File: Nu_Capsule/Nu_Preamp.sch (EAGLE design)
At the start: 20 parts, among them T1 2SC3324, T2 2SC3324

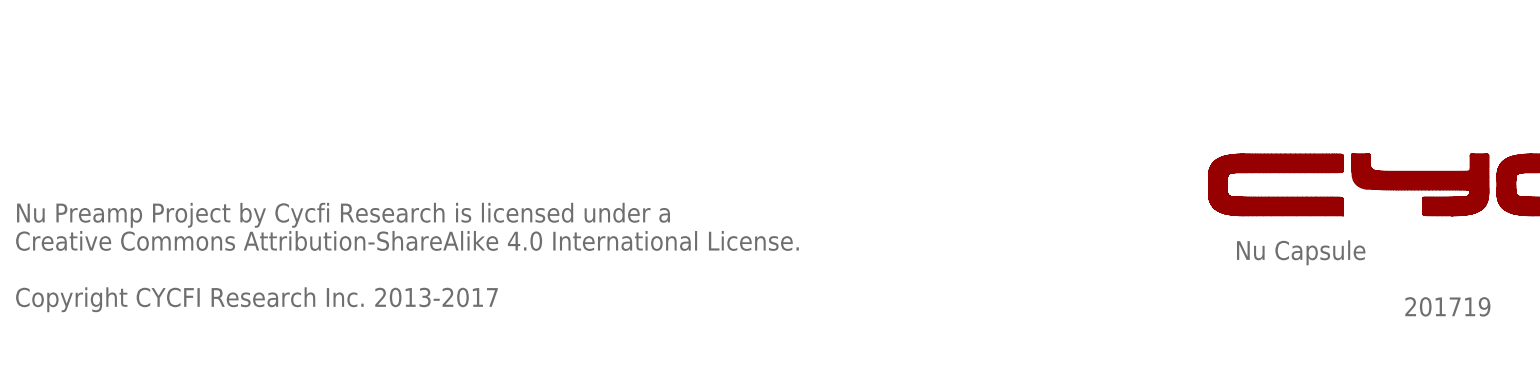
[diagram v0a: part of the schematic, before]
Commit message: Updated Notes "For Nu Project" instead of "Nexus"
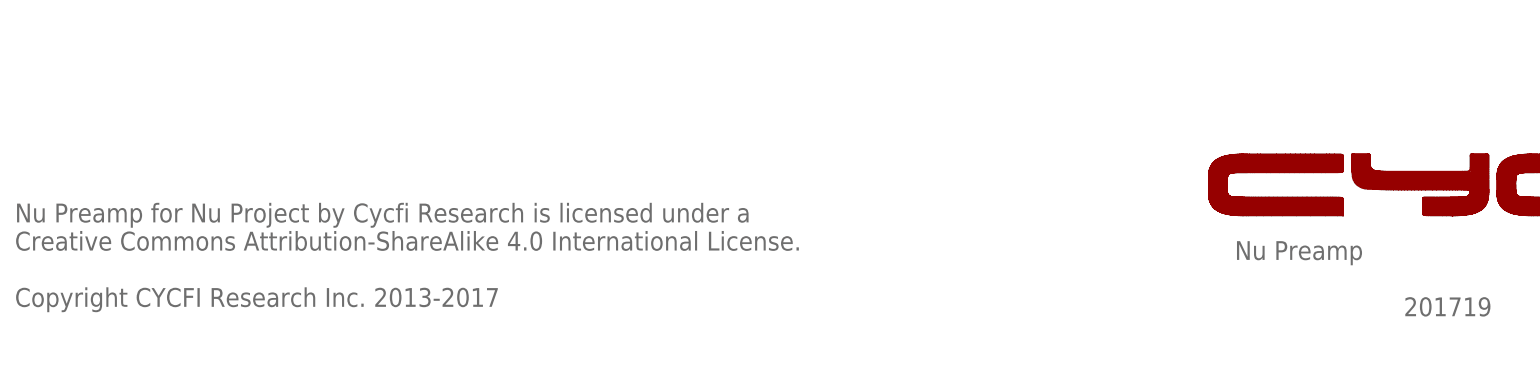
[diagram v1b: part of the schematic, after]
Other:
- note added: "Nu Preamp"
- note added: "Nu Preamp for Nu Project by Cycfi Research is licensed under a Creative Commons Attribution-ShareAlike 4.0 International License. Copyright CYCFI Research Inc. 2013-2017"
- note removed: "Nu Capsule"
- note removed: "Nu Preamp Project by Cycfi Research is licensed under a Creative Commons Attribution-ShareAlike 4.0 International License. Copyright CYCFI Research Inc. 2013-2017"
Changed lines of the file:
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@@
 <?xml version="1.0" encoding="utf-8"?>
 <!DOCTYPE eagle SYSTEM "eagle.dtd">
-<eagle version="6.3">
+<eagle version="7.6.0">
 <drawing>
 <settings>
@@
 <text x="193.04" y="96.8375" size="1.778" layer="95">GND(V-)</text>
 <text x="193.04" y="99.695" size="1.778" layer="95">OUT(O)</text>
-<text x="177.8" y="19.05" size="2.54" layer="95">Nu Capsule</text>
+<text x="177.8" y="19.05" size="2.54" layer="95">Nu Preamp</text>
 <text x="253.365" y="6.985" size="2.1844" layer="95">v1.5</text>
-<text x="12.7" y="12.7" size="2.54" layer="95">Nu Preamp Project by Cycfi Research is licensed under a
+<text x="12.7" y="12.7" size="2.54" layer="95">Nu Preamp for Nu Project by Cycfi Research is licensed under a
 Creative Commons Attribution-ShareAlike 4.0 International License.
 Copyright CYCFI Research Inc. 2013-2017</text>

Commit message: Updated document number.
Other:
- note added: "2017019"
- note removed: "201719"
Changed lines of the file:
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@@
 <text x="193.04" y="99.695" size="1.778" layer="95">OUT(O)</text>
 <text x="177.8" y="19.05" size="2.54" layer="95">Nu Preamp</text>
-<text x="253.365" y="6.985" size="2.1844" layer="95">v1.5</text>
+<text x="253.365" y="6.985" size="2.54" layer="95">v1.5</text>
 <text x="12.7" y="12.7" size="2.54" layer="95">Nu Preamp for Nu Project by Cycfi Research is licensed under a
 Creative Commons Attribution-ShareAlike 4.0 International License.
@@
 <wire x1="90.17" y1="86.995" x2="79.375" y2="86.995" width="0.1524" layer="94"/>
 <wire x1="79.375" y1="86.995" x2="79.375" y2="88.265" width="0.1524" layer="94"/>
-<text x="200.66" y="11.43" size="2.54" layer="95">201719</text>
+<text x="200.66" y="11.43" size="2.54" layer="95">2017019</text>
 <text x="92.71" y="88.9" size="1.778" layer="95">OC</text>
 <text x="92.71" y="95.885" size="1.778" layer="95">IC</text>

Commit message: Updated files for version 2.0
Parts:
- removed C5: 4.7uF, resistor:C-EUC0603
- removed H2: 3P-2MM-TH-MALE, CYCFI_Con:3P-2MM-TH-MALE
- removed PAD18, PAD19, PAD6, PAD7: WIREPADSMD1,27-254, wirepad:WIREPADSMD1,27-254
- removed R7: 4.7K, resistor:R-EU_R0402
- removed T1, T2: 2SC3324, transistor:BC846
- added D1: (no value), m-pad-2.1:D_SCHOTTKYL
- added IC, OC: (no value), wirepad:1,6/0,8
- added U1: OPA209AIDVBR, CYCFI_semicon:OPA209DBVR
- C1: value 4.7uF -> 100pF, 25V; device resistor:C-EUC0603 -> rcl:C-EUC0402
- C2: value 100pF -> 4.7uF, 25V; device resistor:C-EUC0603 -> rcl:C0603_NK
- C3: value 4.7uF -> 0.1uF, 25V; device resistor:C-EUC0603 -> rcl:C-EUC0402
- C4: value 0.1uf -> 4.7uF, 25V; device resistor:C-EUC0603 -> rcl:C-EUC0603
- H1: value 2P-2MM-TH-MALE -> 4P_ZIF_59453-041110EDHLF; device CYCFI_Con:2P-2MM-TH-MALE -> CYCFI_Con:4P_ZIF_59453-041110EDHLF
- R1: value 200K -> 1.2K; device resistor:R-EU_R0603 -> resistor:R-EU_R0402
- R2: value 52.3K -> 1.2K
- R3: value 330 -> 22K
- R4: value 22K -> 47K
- R5: value 10K -> 47K
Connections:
- removed net N$3: C5.2, R5.2, T2.E
- removed net OUTPUT: H1.1, R7.2
- removed net VCVF: R1.2, R4.1, T1.C, T2.B
- removed net VIN: C3.2, C4.2, H2.1, R4.2, T2.C
- new net N$5: C4.1, R3.2, U1G$1.OUT
- new net N$6: R1.2, R4.1, R5.2, U1G$1.IN+
- new net N$7: R2.2, R3.1, U1G$1.IN-
- new net VCC: C2.2, C3.2, D1.C, R5.1, U1G$2.V+
- net GND: now also H1.3, R4.2, U1G$2.V-; no longer C4.1, H2.2, H2.3, PAD7.P, R2.1, R3.1, R5.1
- net N$1: now also D1.A, H1.1; no longer C1.2, R1.1, R2.2, T1.B
- net N$2: now also IC.P, R1.1; no longer C2.2, PAD6.P
- net N$4: now also C1.2, OC.P, R2.1; no longer R3.2, T1.E
- net OUT: now also C4.2, H1.4; no longer C5.1, R7.1
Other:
- note added: "20170817"
- note added: "GND"
- note added: "Nu Capsule"
- note added: "Nu Project by Cycfi Research is licensed under a Creative Commons Attribution-NonCommercial 4.0 International License. http://creativecommons.org/licenses/by-nc/4.0/ Copyright CYCFI Research Inc. 2013-2017"
- note added: "OUT"
- note added: "VCC"
- note added: "v2.0"
- note removed: "2017019"
- note removed: "GND(V-)"
- note removed: "IC"
- note removed: "NC: SMD pads used for coil soldering"
- note removed: "Nu Preamp"
- note removed: "Nu Preamp for Nu Project by Cycfi Research is licensed under a Creative Commons Attribution-ShareAlike 4.0 International License. Copyright CYCFI Research Inc. 2013-2017"
- note removed: "OC"
- note removed: "OUT(O)"
- note removed: "VCC(V+)"
- note removed: "v1.5"
- moved on the sheet: C1, C2, C3, C4, R1, R2, R3, R4, R5, R6

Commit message: Updated document number for Nu Preamp v2.0
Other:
- note added: "2018003"
- note removed: "20170817"
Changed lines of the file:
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@@
 <wire x1="81.28" y1="92.075" x2="70.485" y2="92.075" width="0.1524" layer="94"/>
 <wire x1="70.485" y1="92.075" x2="70.485" y2="93.345" width="0.1524" layer="94"/>
-<text x="200.66" y="11.43" size="2.54" layer="95">20170817</text>
+<text x="200.66" y="11.43" size="2.54" layer="95">2018003</text>
 <text x="73.025" y="105.41" size="1.778" layer="95">COIL</text>
 <wire x1="172.72" y1="125.73" x2="172.72" y2="128.27" width="0.1524" layer="94"/>

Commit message: Updated Nu Preamp Files
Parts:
- removed C4: 4.7uF, 25V, rcl:C-EUC0603
- removed IC, OC: (no value), wirepad:1,6/0,8
- removed R1: 1.2K, resistor:R-EU_R0402
- added H2: 3P-2MM-TH-MALE, CYCFI_Con:3P-2MM-TH-MALE
- added Q1, Q2: 2SC3324, CYCFI_semicon:2SC3324
- added R10, R11: 1.2k, rcl:R-EU_R0402
- added R12: 12k, rcl:R-EU_R0402
- added R13, R15: 100k, rcl:R-EU_R0402
- added R14, R16: 51k, rcl:R-EU_R0402
- added R7: 150k, resistor:R-EU_R0402
- added R8, R9: 33k, rcl:R-EU_R0402
- C1: value 100pF, 25V -> 0.1uF, 25V
- C3: value 0.1uF, 25V -> 10uF, 25V; device rcl:C-EUC0402 -> rcl:C0603_NK
- H1: value 4P_ZIF_59453-041110EDHLF -> 2P-2MM-TH-MALE; device CYCFI_Con:4P_ZIF_59453-041110EDHLF -> CYCFI_Con:2P-2MM-TH-MALE
- R2: value 1.2K -> 10k; device resistor:R-EU_R0402 -> rcl:R-EU_R0402
- R3: value 22K -> 75k
- R4, R5: value 47K -> 33k
- R6: value 10K -> 150k
- U1: value OPA209AIDVBR -> TLV170; device CYCFI_semicon:OPA209DBVR -> CYCFI_semicon:TLV170
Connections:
- removed net N$2: C1.1, IC.P, R1.1
- removed net N$4: C1.2, OC.P, R2.1
- removed net N$7: R2.2, R3.1, U1G$1.IN-
- removed net OUT: C4.2, H1.4, R6.2
- removed net VCC: C2.2, C3.2, D1.C, R5.1, U1G$2.V+
- new net IN+: Q1.B, R13.1, R14.2
- new net IN-: Q2.B, R15.1, R16.2
- new net N$10: Q2.E, R11.2
- new net N$13: R10.1, R11.1, R12.2
- new net N$14: R5.2, R6.1, R7.2, U1G$1.IN+
- new net N$15: R3.2, R4.2, U1G$1.IN-
- new net N$16: C3.1, R3.1, U1G$1.OUT
- new net N$19: D1.A, H2.1
- new net N$9: Q1.E, R10.2
- new net VCC1: C1.1, C2.2, D1.C, R13.2, R15.2, R7.1, R8.2, R9.2, U1G$2.V+
- net GND: now also C1.2, H2.2, H2.3, R12.1, R14.1, R16.1, R2.1, R6.2; no longer C3.1, H1.3, R4.2, R6.1
- net N$1: now also C3.2, R2.2; no longer D1.A
- net N$5: now also Q1.C, R5.1, R8.1; no longer C4.1, R3.2, U1G$1.OUT
- net N$6: now also Q2.C, R9.1; no longer R1.2, R5.2, U1G$1.IN+
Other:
- note added: "GND(V-)"
- note added: "IN+"
- note added: "IN-"
- note added: "Nu Preamp"
- note added: "Nu Project by Cycfi Research is licensed under a Creative Commons Attribution-ShareAlike 4.0 International License. http://creativecommons.org/licenses/by-nc/4.0/ Copyright CYCFI Research Inc. 2013-2018"
- note added: "OUT(O)"
- note added: "VCC(V+)"
- note added: "v2.1"
- note removed: "2018003"
- note removed: "GND"
- note removed: "NOTES: *IC=Inner terminal of the coil *OC=Outer terminal of the coil"
- note removed: "Nu Capsule"
- note removed: "Nu Project by Cycfi Research is licensed under a Creative Commons Attribution-NonCommercial 4.0 International License. http://creativecommons.org/licenses/by-nc/4.0/ Copyright CYCFI Research Inc. 2013-2017"
- note removed: "OUT"
- note removed: "VCC=5V"
- note removed: "v2.0"
- moved on the sheet: C1, C2, C3, D1, R2, R3, R4, R5, R6

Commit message: Document number added
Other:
- note added: "2018004"
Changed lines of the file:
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@@
 <setting verticaltext="up"/>
 </settings>
-<grid distance="0.1" unitdist="inch" unit="inch" style="lines" multiple="1" display="no" altdistance="0.01" altunitdist="inch" altunit="inch"/>
+<grid distance="0.025" unitdist="inch" unit="inch" style="lines" multiple="1" display="yes" altdistance="0.01" altunitdist="inch" altunit="inch"/>
 <layers>
 <layer number="1" name="Top" color="4" fill="1" visible="no" active="no"/>
@@
 <wire x1="18.415" y1="94.615" x2="23.495" y2="94.615" width="0.1524" layer="94"/>
 <wire x1="18.415" y1="89.535" x2="23.495" y2="89.535" width="0.1524" layer="94"/>
+<text x="200.025" y="11.43" size="2.54" layer="95">2018004</text>
 </plain>
 <instances>

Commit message: Updated files for Nu Preamp v2.1.1 added
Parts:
- added GND, IN+, IN-: (no value), wirepad:SMD2
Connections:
- net GND: now also GND.P
- net IN+: now also IN+.P
- net IN-: now also IN-.P
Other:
- note added: "2018005"
- note removed: "2018004"
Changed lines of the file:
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@@
 <setting verticaltext="up"/>
 </settings>
-<grid distance="0.025" unitdist="inch" unit="inch" style="lines" multiple="1" display="yes" altdistance="0.01" altunitdist="inch" altunit="inch"/>
+<grid distance="0.1" unitdist="inch" unit="inch" style="lines" multiple="1" display="no" altdistance="0.01" altunitdist="inch" altunit="inch"/>
 <layers>
 <layer number="1" name="Top" color="4" fill="1" visible="no" active="no"/>
@@
 <part name="SUPPLY1" library="supply2" deviceset="GND" device=""/>
 <part name="C2" library="rcl" deviceset="C0603_NK" device="" value="4.7uF, 25V"/>
+<part name="IN+" library="wirepad" deviceset="SMD2" device=""/>
+<part name="IN-" library="wirepad" deviceset="SMD2" device=""/>
+<part name="GND" library="wirepad" deviceset="SMD2" device=""/>
 </parts>
 <sheets>
@@
 <wire x1="18.415" y1="94.615" x2="23.495" y2="94.615" width="0.1524" layer="94"/>
 <wire x1="18.415" y1="89.535" x2="23.495" y2="89.535" width="0.1524" layer="94"/>
-<text x="200.025" y="11.43" size="2.54" layer="95">2018004</text>
+<text x="200.025" y="11.43" size="2.54" layer="95">2018005</text>
 </plain>
 <instances>
@@
 <attribute name="VALUE" x="95.504" y="129.54" size="1.778" layer="96"/>
 </instance>
+<instance part="IN+" gate="1" x="25.4" y="170.18" smashed="yes">
+<attribute name="NAME" x="19.177" y="169.4942" size="1.778" layer="95"/>
+<attribute name="VALUE" x="24.257" y="166.878" size="1.778" layer="96"/>
+</instance>
+<instance part="IN-" gate="1" x="25.4" y="162.56" smashed="yes">
+<attribute name="NAME" x="19.177" y="161.8742" size="1.778" layer="95"/>
+<attribute name="VALUE" x="24.257" y="159.258" size="1.778" layer="96"/>
+</instance>
+<instance part="GND" gate="1" x="25.4" y="154.94" smashed="yes">
+<attribute name="NAME" x="18.923" y="154.0002" size="1.778" layer="95"/>
+<attribute name="VALUE" x="24.257" y="151.638" size="1.778" layer="96"/>
+</instance>
 </instances>
 <busses>
@@
 <wire x1="23.495" y1="94.615" x2="39.37" y2="94.615" width="0.1524" layer="91"/>
 </segment>
+<segment>
+<pinref part="IN+" gate="1" pin="P"/>
+<wire x1="27.94" y1="170.18" x2="30.48" y2="170.18" width="0.1524" layer="91"/>
+<label x="33.02" y="170.18" size="1.778" layer="95"/>
+</segment>
 </net>
 <net name="IN-" class="0">
@@
 <wire x1="90.805" y1="45.085" x2="90.805" y2="94.615" width="0.1524" layer="91"/>
 <wire x1="90.805" y1="94.615" x2="81.28" y2="94.615" width="0.1524" layer="91"/>
+</segment>
+<segment>
+<pinref part="IN-" gate="1" pin="P"/>
+<wire x1="27.94" y1="162.56" x2="30.48" y2="162.56" width="0.1524" layer="91"/>
+<label x="33.02" y="162.56" size="1.778" layer="95"/>
 </segment>
 </net>
@@
 <wire x1="102.87" y1="125.73" x2="102.87" y2="129.54" width="0.1524" layer="91"/>
 </segment>
+<segment>
+<pinref part="GND" gate="1" pin="P"/>
+<wire x1="27.94" y1="154.94" x2="30.48" y2="154.94" width="0.1524" layer="91"/>
+<label x="33.02" y="154.94" size="1.778" layer="95"/>
+</segment>
 </net>
